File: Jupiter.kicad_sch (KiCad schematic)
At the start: 341 parts, among them J1 Conn_01x04, SW1 SW_Push, U1 ATmega32U4-M, Y1 Crystal_GND24_Small

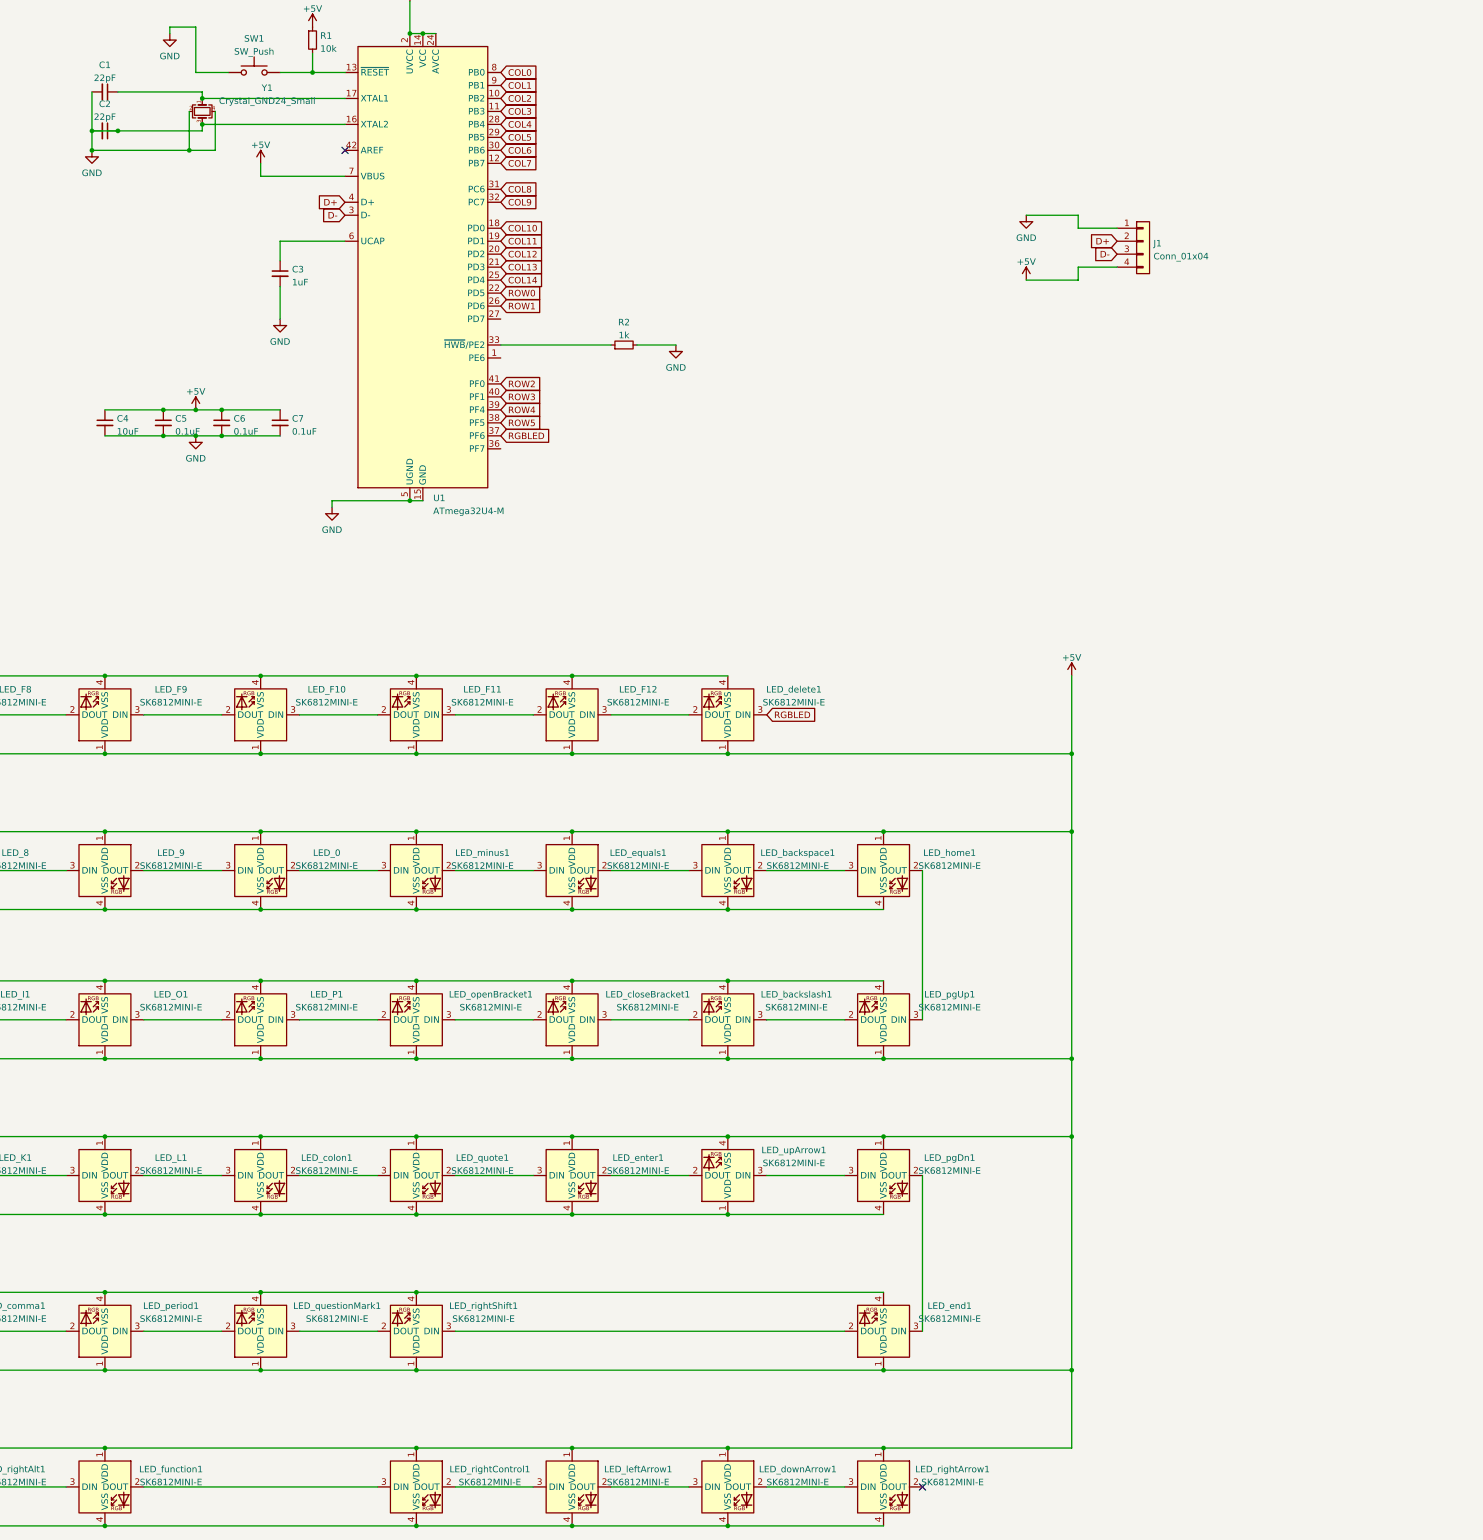
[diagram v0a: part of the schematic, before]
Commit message: Finished LED capacitor placement
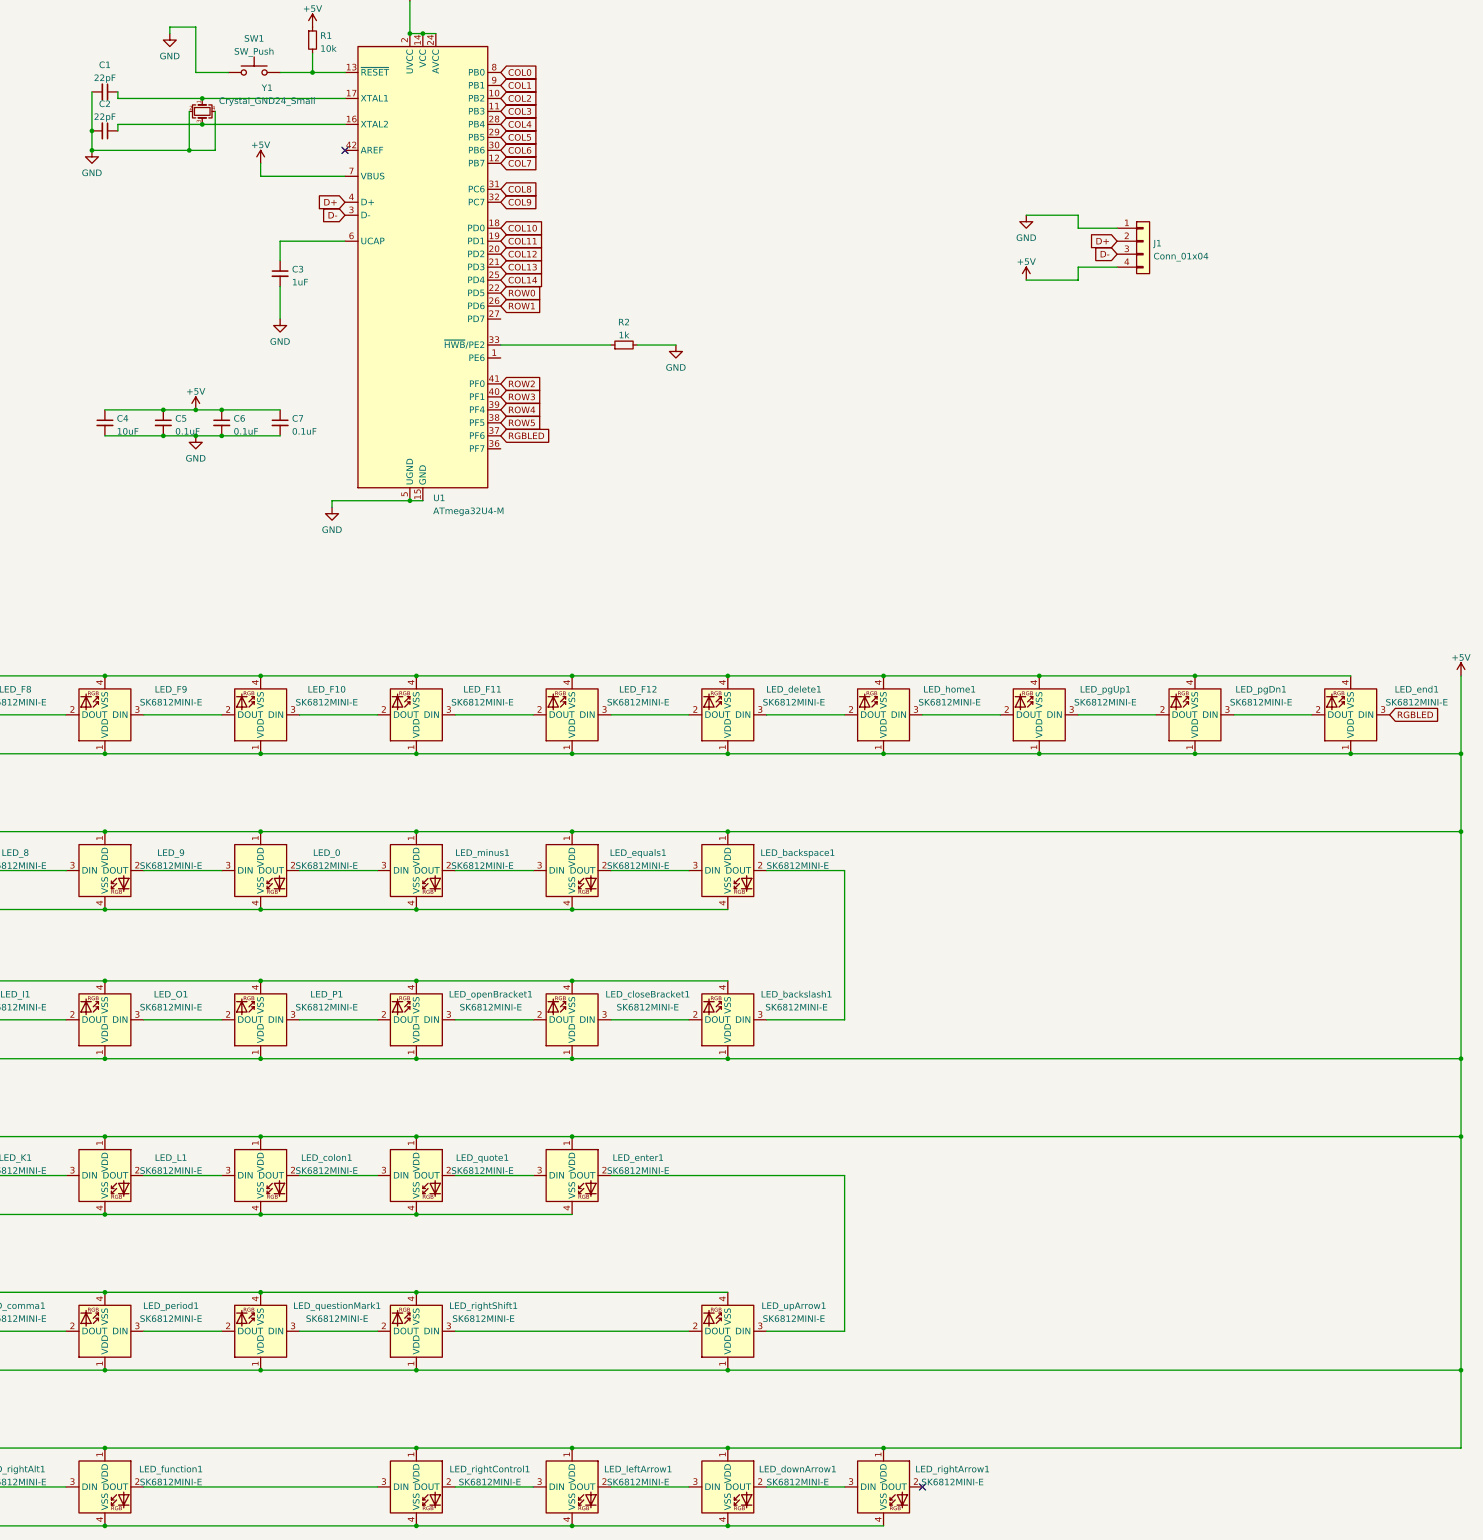
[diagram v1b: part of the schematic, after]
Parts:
- LED_0, LED_1, LED_2, LED_3, LED_4, LED_5, LED_6, LED_7, LED_8, LED_9, LED_A1, LED_D1, LED_F13, LED_G1, LED_H1, LED_J1, LED_K1, LED_L1, LED_S1, LED_backspace1, LED_capsLock1, LED_colon1, LED_downArrow1, LED_end1, LED_enter1, LED_equals1, LED_function1, LED_leftAlt1, LED_leftArrow1, LED_leftControl1, LED_minus1, LED_pgDn1, LED_pgUp1, LED_quote1, LED_rightAlt1, LED_rightArrow1, LED_rightControl1, LED_space1, LED_tilda1, LED_windows1: footprint marbastlib-mx:LED_MX_6028R -> marbastlib-mx:LED_MX_6028R-FLIPPED
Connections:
- net +5V: now also LED_upArrow1.1 (VDD); no longer LED_upArrow1.4 (VSS)
- net GND: now also LED_upArrow1.4 (VSS); no longer C2.1, LED_upArrow1.1 (VDD), U1.16 (XTAL2), Y1.3
- net RGBLED: now also LED_end1.3 (DIN); no longer LED_delete1.3 (DIN)
- net at LED_rightShift1.3 (DIN): now also LED_upArrow1.2 (DOUT); no longer LED_end1.2 (DOUT)
- net at LED_pgDn1.2 (DOUT): now also LED_pgUp1.3 (DIN); no longer LED_end1.3 (DIN)
- net at LED_home1.2 (DOUT): now also LED_delete1.3 (DIN); no longer LED_pgUp1.3 (DIN)
- net at LED_backspace1.2 (DOUT): now also LED_backslash1.3 (DIN); no longer LED_home1.3 (DIN)
- net at LED_enter1.2 (DOUT): now also LED_upArrow1.3 (DIN); no longer LED_upArrow1.2 (DOUT)
- net at LED_pgDn1.3 (DIN): now also LED_end1.2 (DOUT); no longer LED_upArrow1.3 (DIN)
- net at LED_pgUp1.2 (DOUT): now also LED_home1.3 (DIN); no longer LED_backslash1.3 (DIN)
- new net: C2.1, U1.16 (XTAL2), Y1.3

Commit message: traces
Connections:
- net COL0: now also U1.40 (PF1); no longer U1.8 (PB0)
- net COL1: now also U1.38 (PF5); no longer U1.9 (PB1)
- net COL11: now also U1.22 (PD5); no longer U1.19 (PD1)
- net COL2: now also U1.37 (PF6); no longer U1.10 (PB2)
- net COL3: now also U1.36 (PF7); no longer U1.11 (PB3)
- net COL7: now also U1.19 (PD1); no longer U1.12 (PB7)
- net RGBLED: now also U1.12 (PB7); no longer U1.37 (PF6)
- net ROW0: now also U1.41 (PF0); no longer U1.22 (PD5)
- net ROW1: now also U1.39 (PF4); no longer U1.26 (PD6)
- net ROW2: now also U1.9 (PB1); no longer U1.41 (PF0)
- net ROW3: now also U1.8 (PB0); no longer U1.40 (PF1)
- net ROW4: now also U1.10 (PB2); no longer U1.39 (PF4)
- net ROW5: now also U1.11 (PB3); no longer U1.38 (PF5)

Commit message: more traces
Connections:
- net COL10: now also U1.26 (PD6); no longer U1.18 (PD0)
- net COL11: now also U1.25 (PD4); no longer U1.22 (PD5)
- net COL12: now also U1.22 (PD5); no longer U1.20 (PD2)
- net COL14: now also U1.9 (PB1); no longer U1.25 (PD4)
- net COL4: now also U1.32 (PC7); no longer U1.28 (PB4)
- net COL5: now also U1.31 (PC6); no longer U1.29 (PB5)
- net COL7: now also U1.29 (PB5); no longer U1.19 (PD1)
- net COL8: now also U1.28 (PB4); no longer U1.31 (PC6)
- net COL9: now also U1.27 (PD7); no longer U1.32 (PC7)
- net ROW2: now also U1.20 (PD2); no longer U1.9 (PB1)

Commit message: almost finished trace routing
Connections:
- net ROW3: now also U1.19 (PD1); no longer U1.8 (PB0)
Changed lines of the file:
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@@
+    )
+  )
+  (global_label "ROW3" (shape input) (at 391.16 67.31 0) (fields_autoplaced)
+    (effects (font (size 1.27 1.27)) (justify left))
+    (property "Intersheet References" "${INTERSHEET_REFS}" (id 0) (at 398.8345 67.3894 0)
+      (effects (font (size 1.27 1.27)) (justify left) hide)
     )
   )
@@
       (effects (font (size 1.27 1.27)) (justify left) hide)
     )
-  )
-  (global_label "ROW3" (shape input) (at 391.16 34.29 0) (fields_autoplaced)
-    (effects (font (size 1.27 1.27)) (justify left))
-    (property "Intersheet References" "${INTERSHEET_REFS}" (id 0) (at 398.8345 34.3694 0)
-      (effects (font (size 1.27 1.27)) (justify left) hide)
-    )

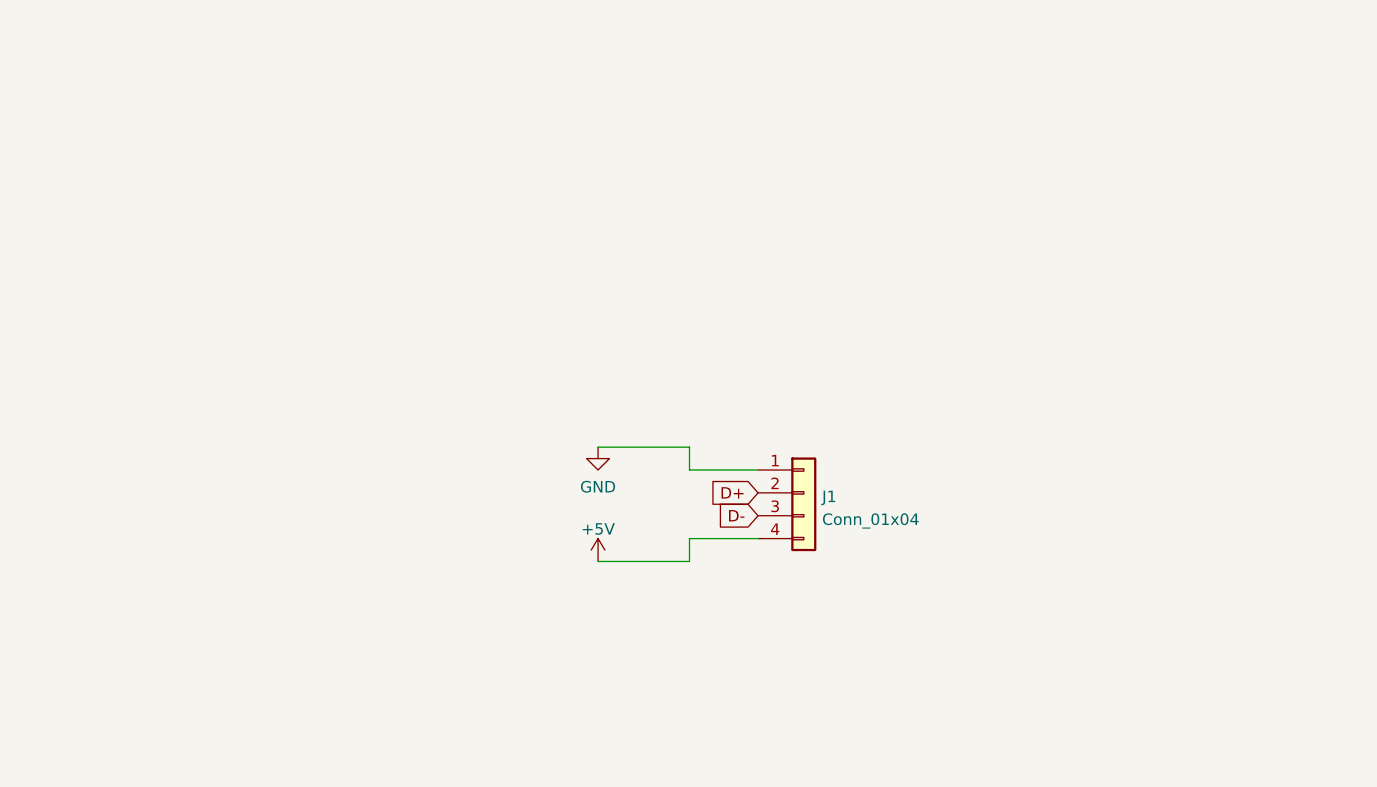
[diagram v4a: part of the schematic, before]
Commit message: Added usb connector
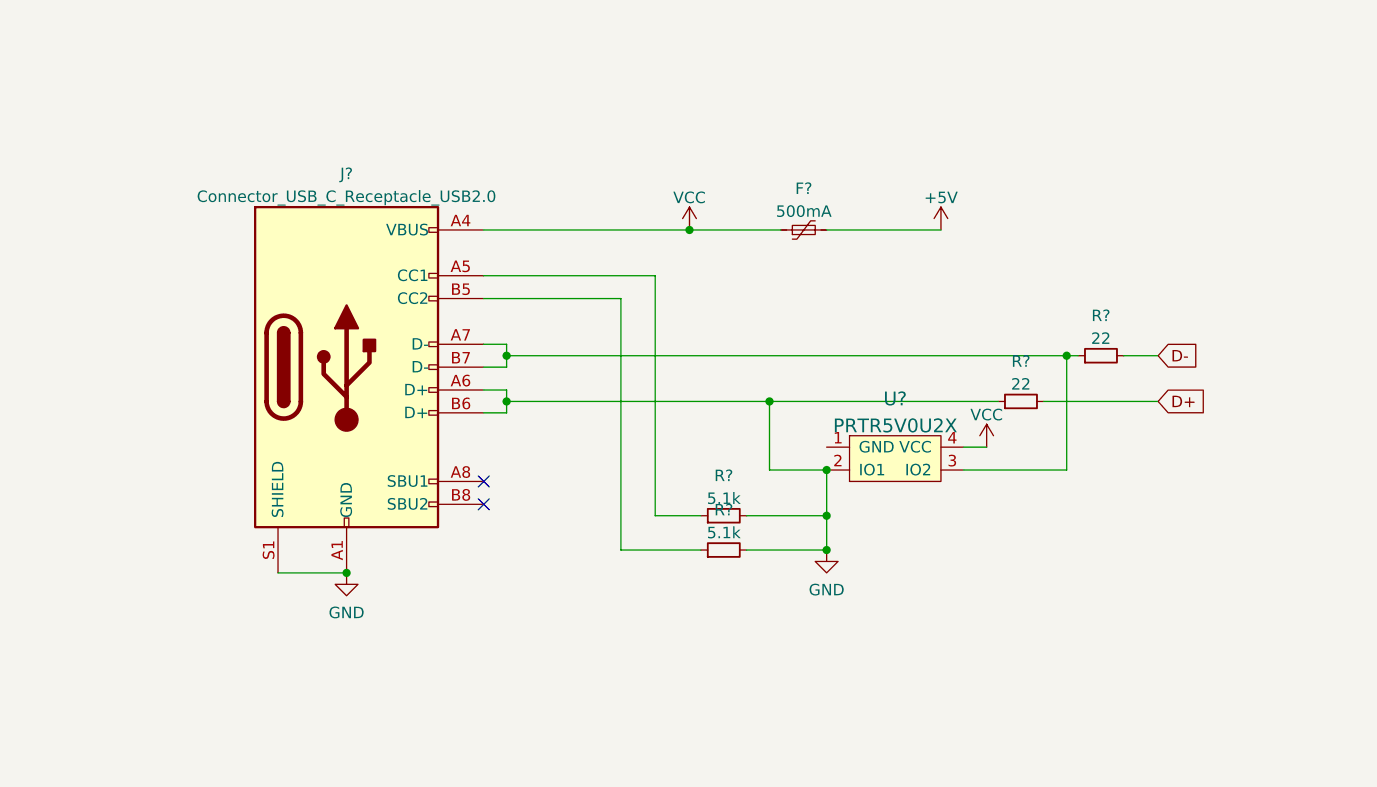
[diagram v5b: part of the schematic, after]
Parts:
- removed J1: Conn_01x04, random-keyboard-parts:JST-SR-4, symbol Connector_Generic:Conn_01x04
- added F?: 500mA, symbol Device:Polyfuse_Small
- added J?: Connector_USB_C_Receptacle_USB2.0, symbol USB-C-USB-2.0-cache:Connector_USB_C_Receptacle_USB2.0
- added R? (x2): 5.1k, symbol Device:R_Small
- added R? (x2): 22, symbol Device:R_Small
- added U?: PRTR5V0U2X, symbol random-keyboard-parts:PRTR5V0U2X
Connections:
- net +5V: now also F?.2
- net D+: now also R?.2
- net D-: now also R?.2
- net GND: now also J?.A1 (GND), J?.A12 (GND), J?.A6 (D+), J?.B1 (GND), J?.B12 (GND), J?.B6 (D+), J?.S1 (SHIELD), R?.1, R?.2, R?.2, U?.2 (IO1)
- new net: J?.A5 (CC1), R?.1
- new net: J?.A7 (D-), J?.B7 (D-), R?.1, U?.3 (IO2)
- new net: J?.B5 (CC2), R?.1
- new net VBUS: F?.1, J?.A4 (VBUS), J?.A9 (VBUS), J?.B4 (VBUS), J?.B9 (VBUS), U?.4 (VCC)
- no-connect marks 2 -> 4
